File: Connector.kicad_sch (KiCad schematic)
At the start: 13 parts, among them J1 TC2070-IDC-NL, J10 JST_XH_S2B-A, J2 XT30PW-M, J3 JST_XH_S4B-A, J4 JST_XH_S2B-A, J5 JST_XH_S2B-A, J6 JST_XH_S2B-A, J7 JST_XH_S2B-A, J8 JST_XH_S3B, J9 JST_XH_S4B-A, SW2 OS102011MA1Q

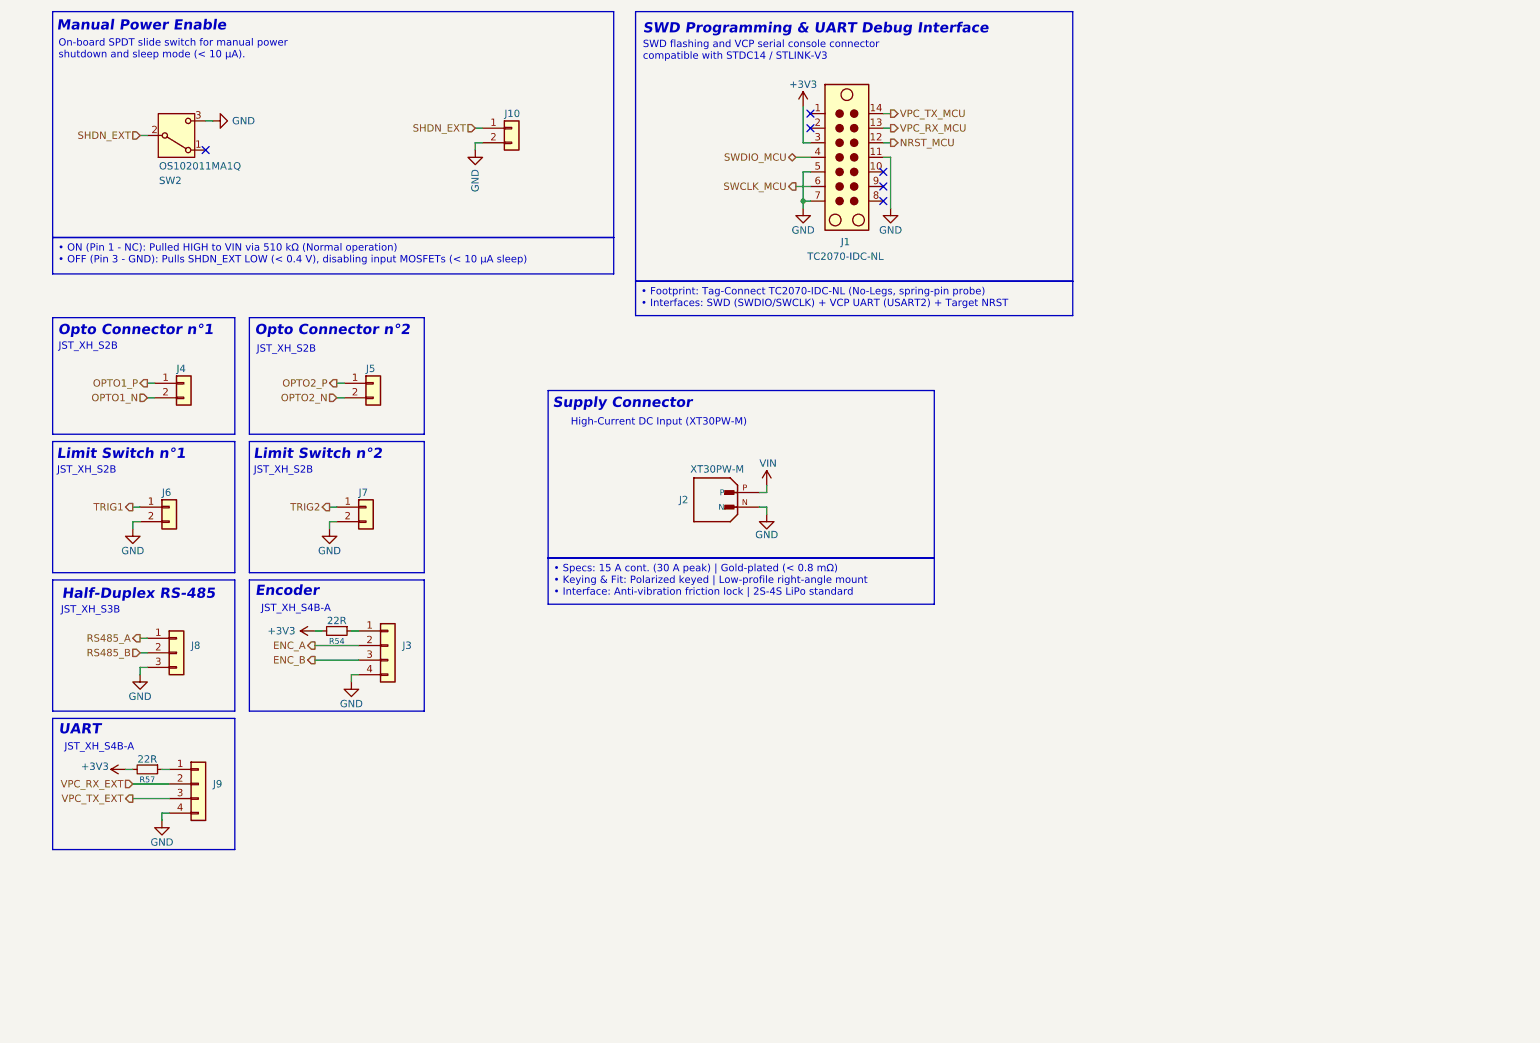
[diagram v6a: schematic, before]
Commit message: feat : add SMLVN6RGB status LED stage with balanced 3.3V ballast resistors
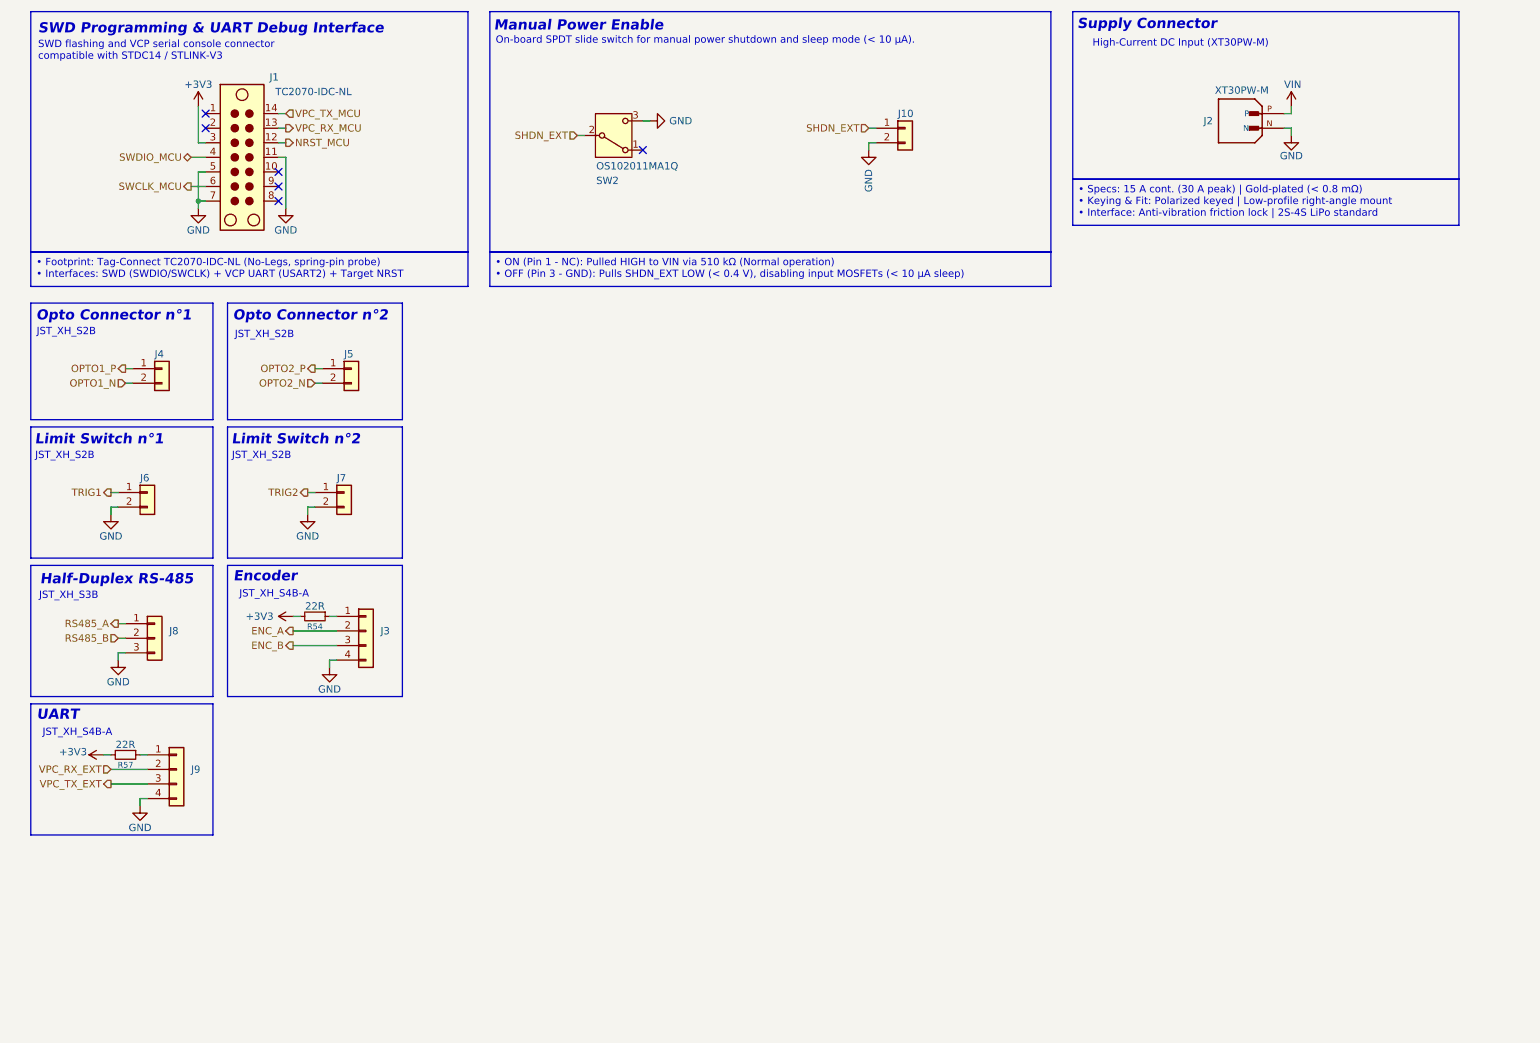
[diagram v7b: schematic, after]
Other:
- moved on the sheet: J1, J10, J2, J3, J4, J5, J6, J7, J8, J9, R54, R57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

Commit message: feat: switch to JST-GH connectors and add TPD4E05U06 TVS protection for SPI/I2C
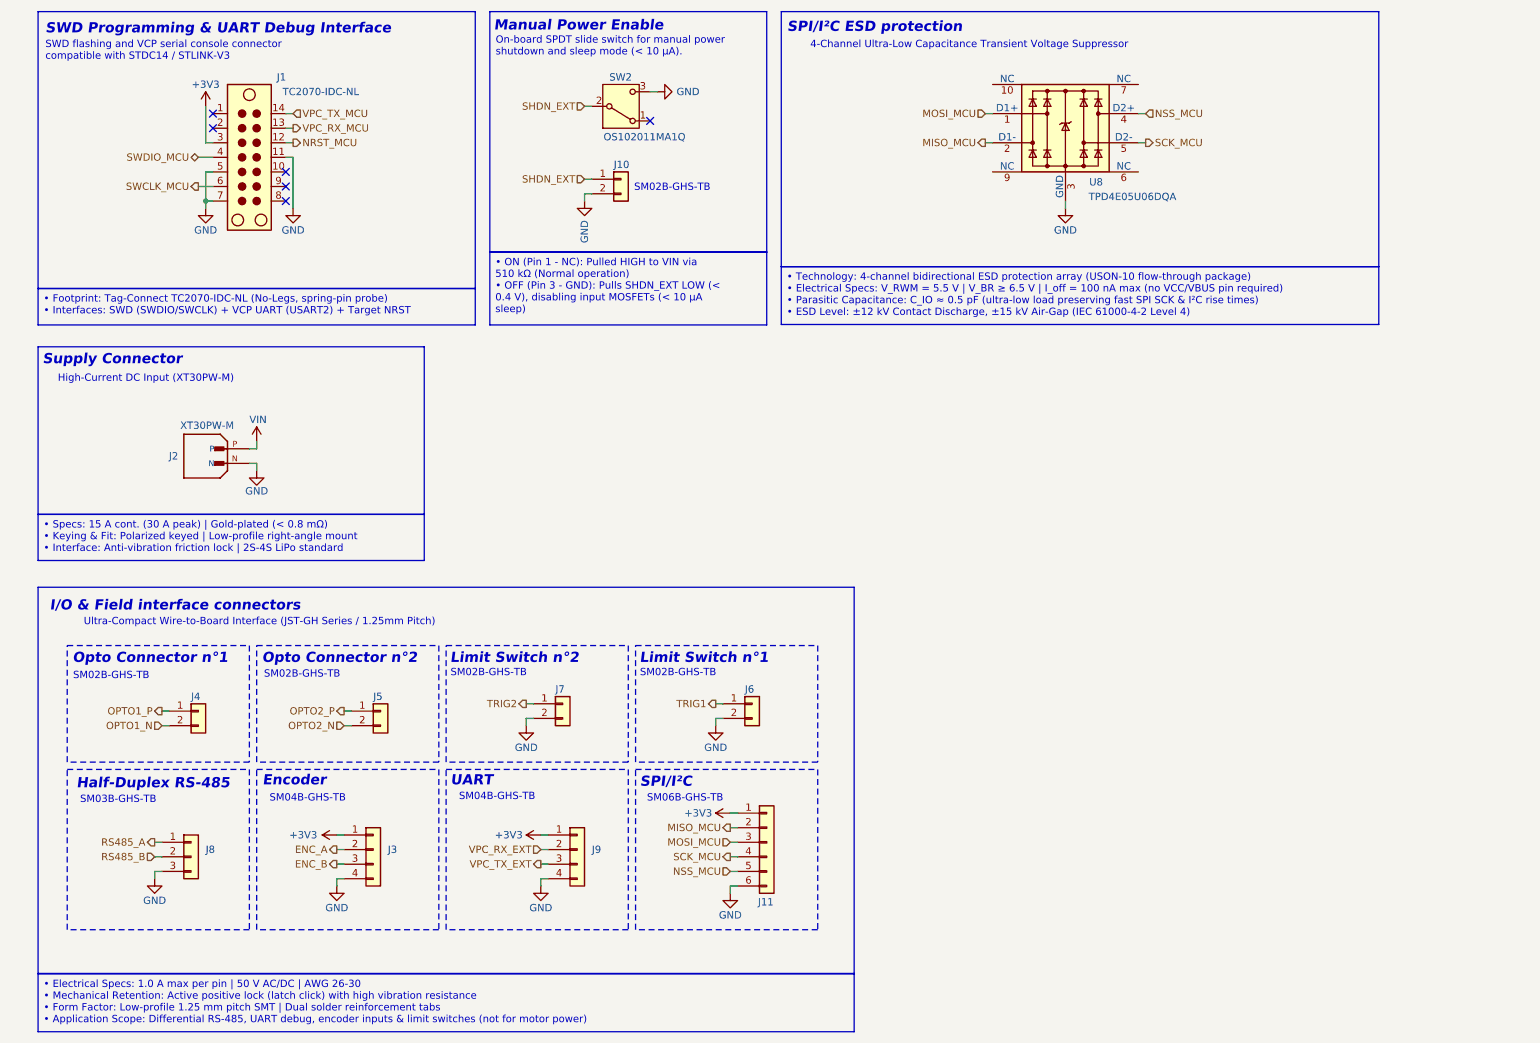
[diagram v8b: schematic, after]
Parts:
- removed R54, R57: 22R, Resistor_SMD:R_0603_1608Metric, symbol Device:R_Small
- added J11: Conn_01x06, Connector_JST:JST_GH_SM06B-GHS-TB_1x06-1MP_P1.25mm_Horizontal, symbol Connector_Generic:Conn_01x06
- added U8: TPD4E05U06DQA, Package_SON:USON-10_2.5x1.0mm_P0.5mm, symbol Power_Protection:TPD4E05U06DQA
- J10, J4, J6, J7: value JST_XH_S2B-A -> SM02B-GHS-TB; footprint Connector_JST:JST_XH_S2B-XH-A_1x02_P2.50mm_Horizontal -> Connector_JST:JST_GH_SM02B-GHS-TB_1x02-1MP_P1.25mm_Horizontal
- J3, J9: value JST_XH_S4B-A -> SM04B-GHS-TB; footprint Connector_JST:JST_XH_S4B-XH-A-1_1x04_P2.50mm_Horizontal -> Connector_JST:JST_GH_SM04B-GHS-TB_1x04-1MP_P1.25mm_Horizontal
- J5: value JST_XH_S2B-A -> BM02B-GHS-TBT
- J8: value JST_XH_S3B -> SM03B-GHS-TB; footprint Connector_JST:JST_XH_S3B-XH-A-1_1x03_P2.50mm_Horizontal -> Connector_JST:JST_GH_SM03B-GHS-TB_1x03-1MP_P1.25mm_Horizontal
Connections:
- net +3V3: now also J3.1 (Pin_1), J9.1 (Pin_1), J11.1 (Pin_1)
- net GND: now also J11.6 (Pin_6), U8.3 (GND), U8.8 (GND)
- new net MISO_MCU: J11.2 (Pin_2), U8.2 (D1-)
- new net MOSI_MCU: J11.3 (Pin_3), U8.1 (D1+)
- new net NSS_MCU: J11.5 (Pin_5), U8.4 (D2+)
- new net SCK_MCU: J11.4 (Pin_4), U8.5 (D2-)
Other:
- note added: "4-Channel Ultra-Low Capacitance Transient Voltage Suppressor"
- note added: "I/O & Field interface connectors"
- note added: "SM02B-GHS-TB"
- note added: "SM03B-GHS-TB"
- note added: "SM04B-GHS-TB"
- note added: "SM06B-GHS-TB"
- note added: "SPI/I²C"
- note added: "SPI/I²C ESD protection"
- note added: "Ultra-Compact Wire-to-Board Interface (JST-GH Series / 1.25mm Pitch)"
- note removed: "JST_XH_S2B"
- note removed: "JST_XH_S3B"
- note removed: "JST_XH_S4B-A"
- moved on the sheet: J1, J10, J2, J3, J4, J5, J8, SW2
